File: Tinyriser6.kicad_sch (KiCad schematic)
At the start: 24 parts, among them J1 Bus_M.2_Socket_M, J10 Conn_02x04_Odd_Even, J11 Conn_02x04_Odd_Even, J2 Bus_PCI_Express_x16, J3 Conn_02x04_Odd_Even, J6 USB_A, J8 Conn_02x04_Odd_Even, J9 Conn_02x04_Odd_Even, M1 Fan_4pin

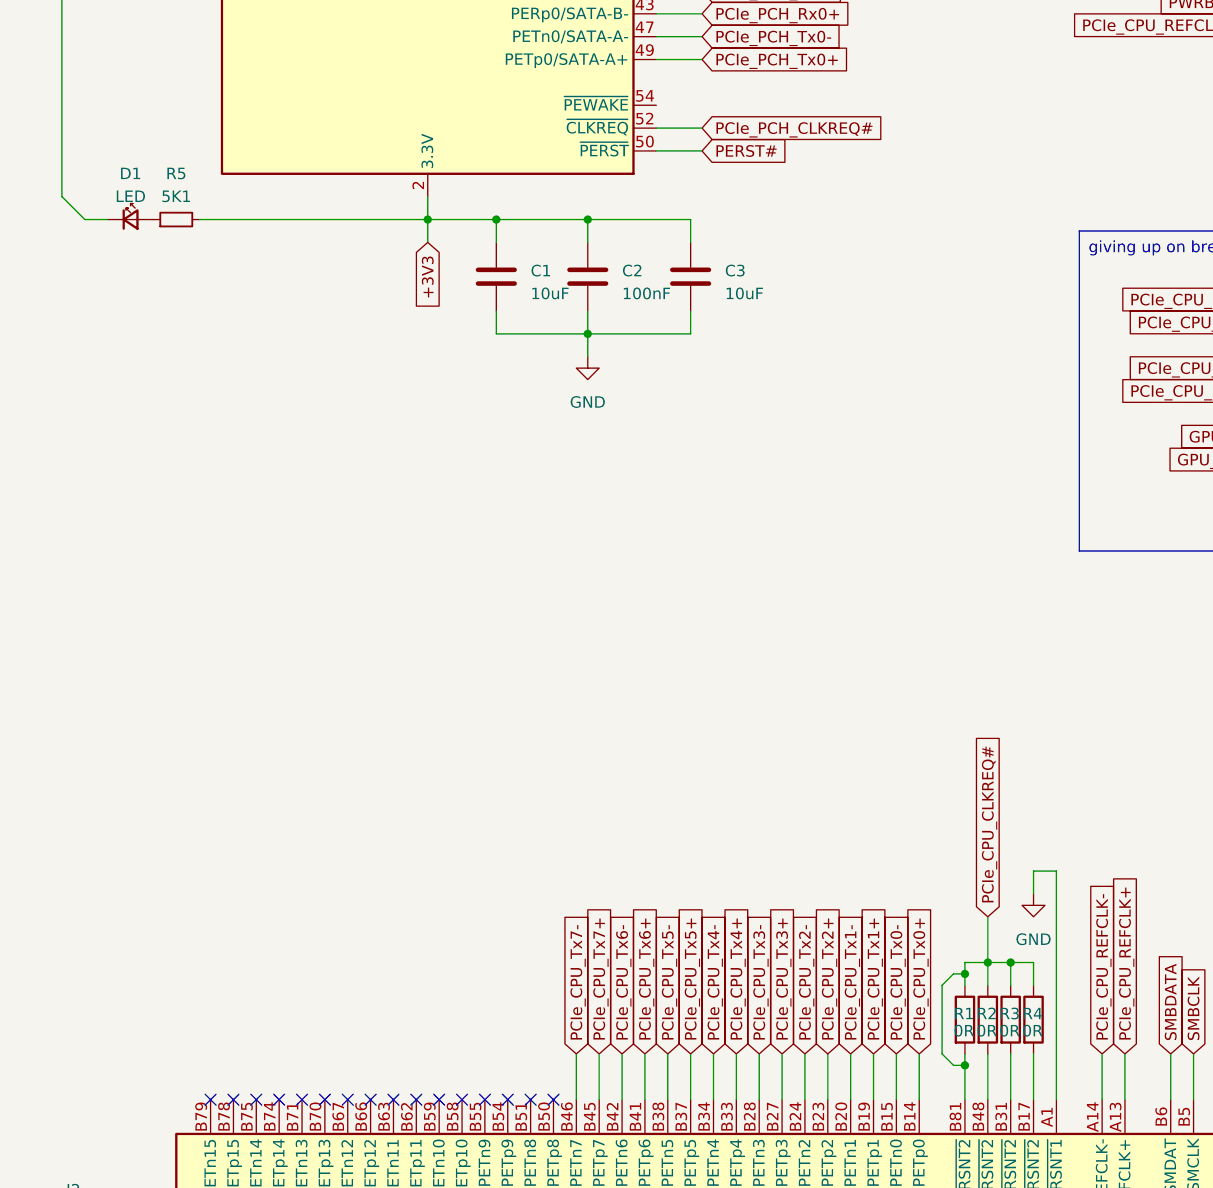
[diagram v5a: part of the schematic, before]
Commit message: changed resistor refdes
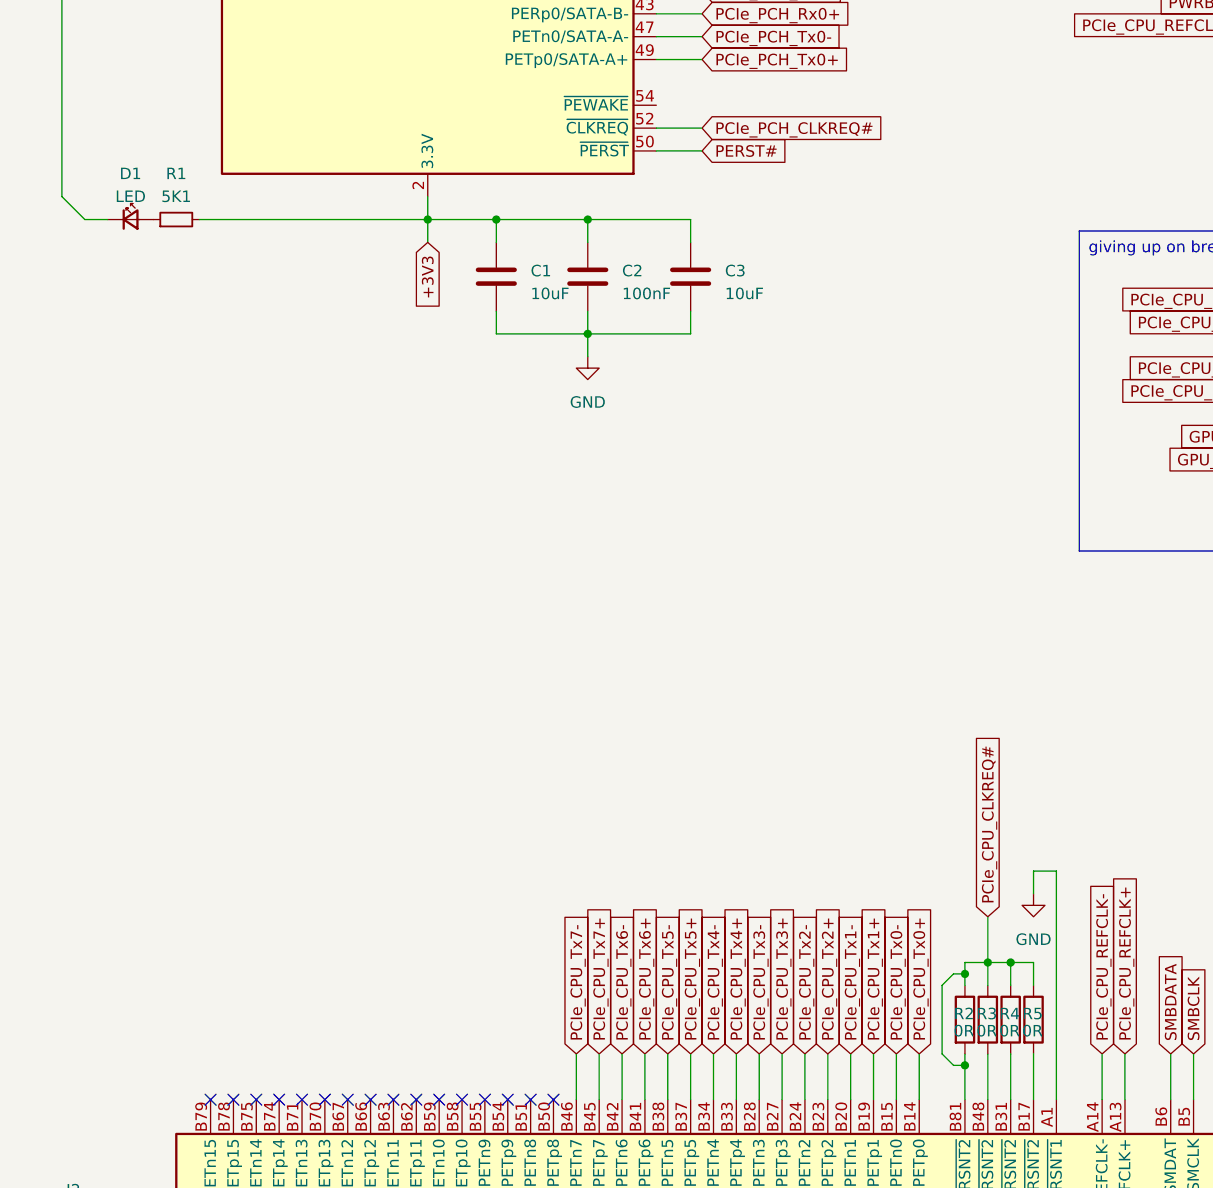
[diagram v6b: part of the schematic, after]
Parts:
- renumbered R5 to R1, R1 to R2, R2 to R3, R3 to R4, R4 to R5

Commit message: giving up on breaking out ESPI, tuned some diffpairs
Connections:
- net ESPI_ALERT0#_BMC: no longer J9.4 (Pin_4)
- net ESPI_ALERT1#: no longer J9.1 (Pin_1)
- net ESPI_CLK_BMC: no longer J11.3 (Pin_3)
- net ESPI_CS0#_BMC: no longer J8.6 (Pin_6)
- net ESPI_CS1#_BMC: no longer J8.5 (Pin_5)
- net ESPI_IO0_BMC: no longer J11.6 (Pin_6)
- net ESPI_IO1_BMC: no longer J10.3 (Pin_3)
- net ESPI_RESET#_BMC: no longer J10.4 (Pin_4)

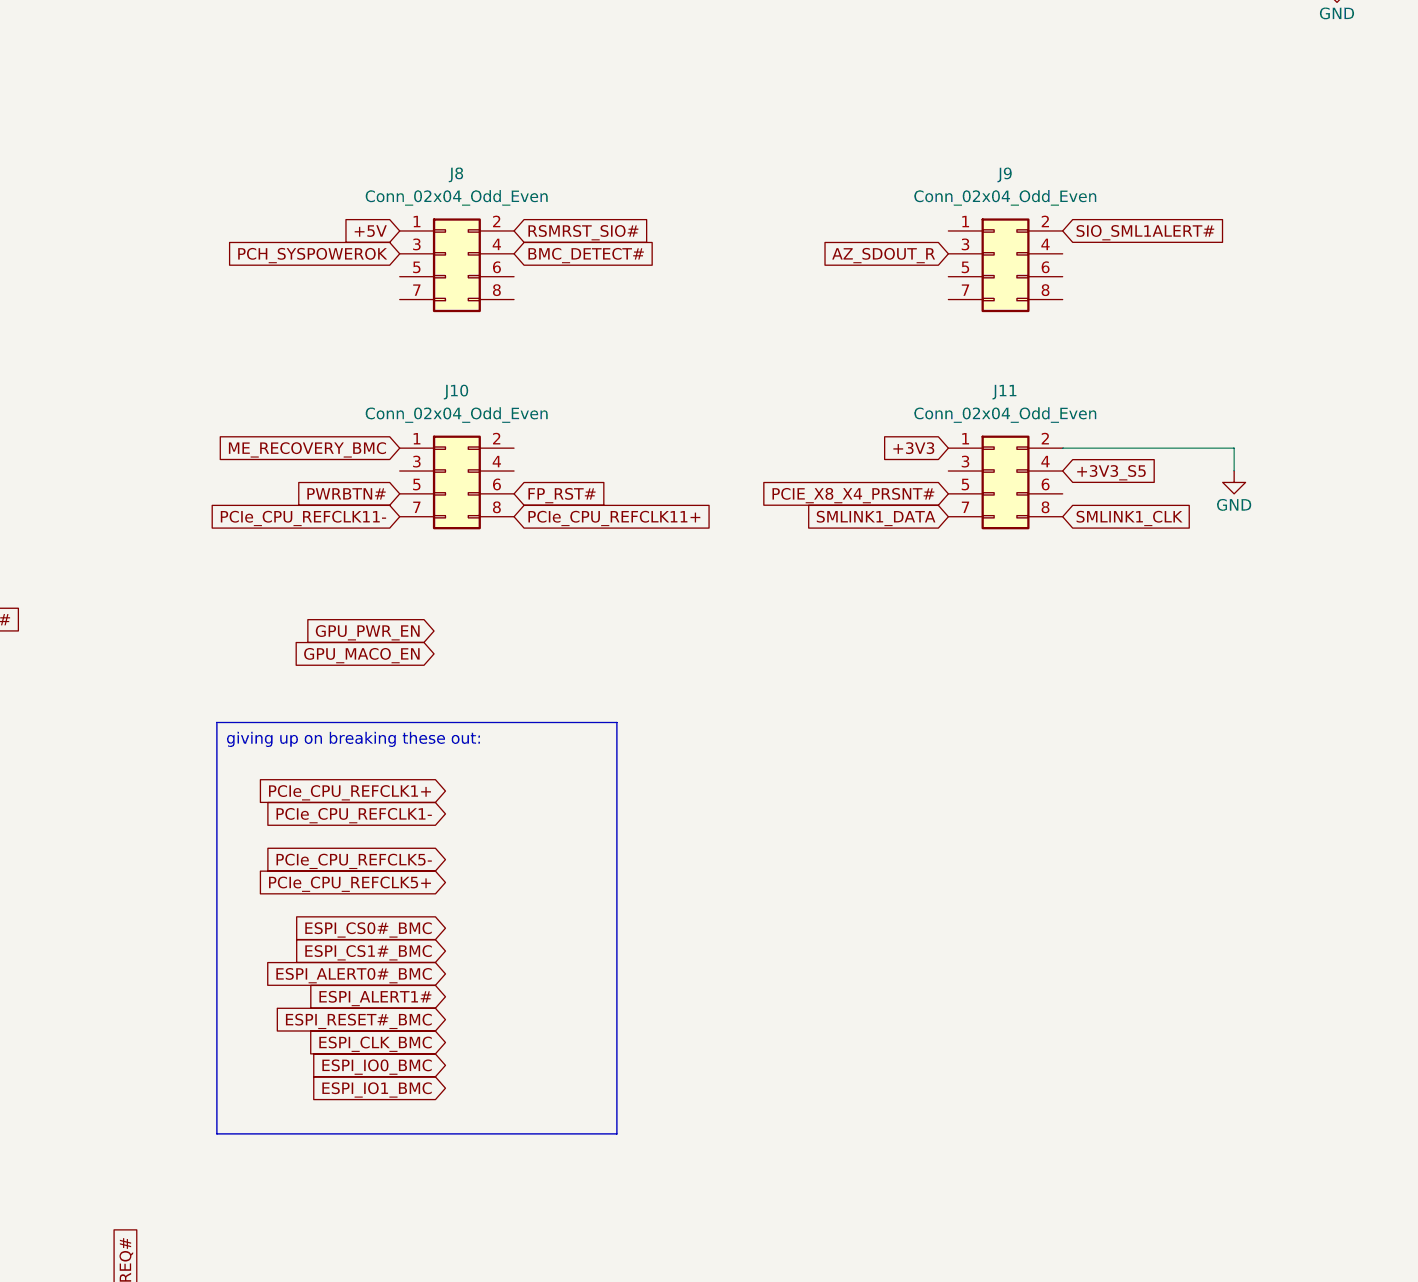
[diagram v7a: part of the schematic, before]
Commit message: Changed misc IO header to 2x10 and started routing it
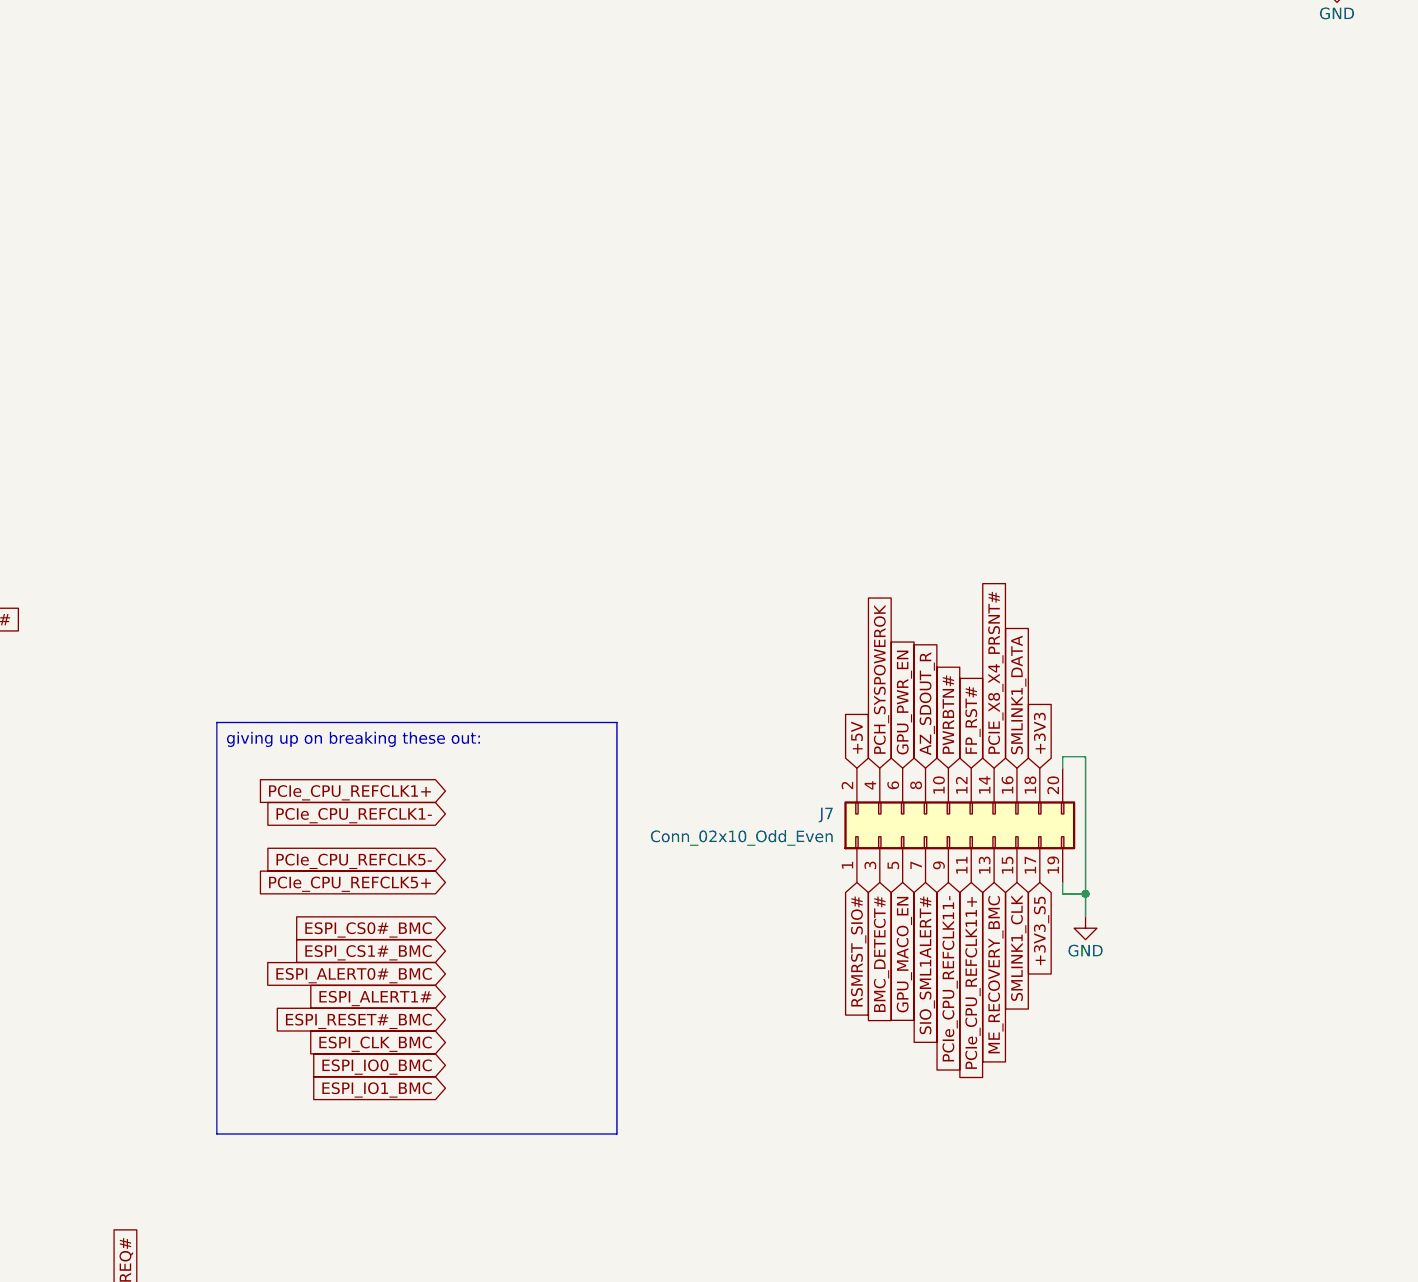
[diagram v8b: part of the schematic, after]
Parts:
- removed J10, J11, J8, J9: Conn_02x04_Odd_Even, Connector_PinHeader_2.00mm:PinHeader_2x04_P2.00mm_Vertical, symbol Connector_Generic:Conn_02x04_Odd_Even
- added J7: Conn_02x10_Odd_Even, Connector_PinHeader_2.00mm:PinHeader_2x10_P2.00mm_Vertical, symbol Connector_Generic:Conn_02x10_Odd_Even
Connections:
- net +3V3: now also J7.18 (Pin_18)
- net +3V3_S5: now also J7.17 (Pin_17)
- net +5V: now also J7.2 (Pin_2)
- net AZ_SDOUT_R: now also J7.8 (Pin_8)
- net BMC_DETECT#: now also J7.3 (Pin_3)
- net FP_RST#: now also J7.12 (Pin_12)
- net GND: now also J7.19 (Pin_19), J7.20 (Pin_20)
- net GPU_MACO_EN: now also J7.5 (Pin_5)
- net GPU_PWR_EN: now also J7.6 (Pin_6)
- net ME_RECOVERY_BMC: now also J7.13 (Pin_13)
- net PCH_SYSPOWEROK: now also J7.4 (Pin_4)
- net PCIE_X8_X4_PRSNT#: now also J7.14 (Pin_14)
- net PCIe_CPU_REFCLK11+: now also J7.11 (Pin_11)
- net PCIe_CPU_REFCLK11-: now also J7.9 (Pin_9)
- net PWRBTN#: now also J7.10 (Pin_10)
- net RSMRST_SIO#: now also J7.1 (Pin_1)
- net SIO_SML1ALERT#: now also J7.7 (Pin_7)
- net SMLINK1_CLK: now also J7.15 (Pin_15)
- net SMLINK1_DATA: now also J7.16 (Pin_16)
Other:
- company: (none) -> WifiCable
- title: (none) -> TinyRiser v1
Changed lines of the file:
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@@
 	(generator_version "8.0")
 	(paper "A3")
+	(title_block
+		(title "TinyRiser v1")
+		(rev "meow")
+		(company "WifiCable")
+		(comment 4 "nya")
+	)
